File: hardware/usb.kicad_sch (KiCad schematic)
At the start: 7 parts, among them J4 USB_C_Receptacle_USB2.0_14P

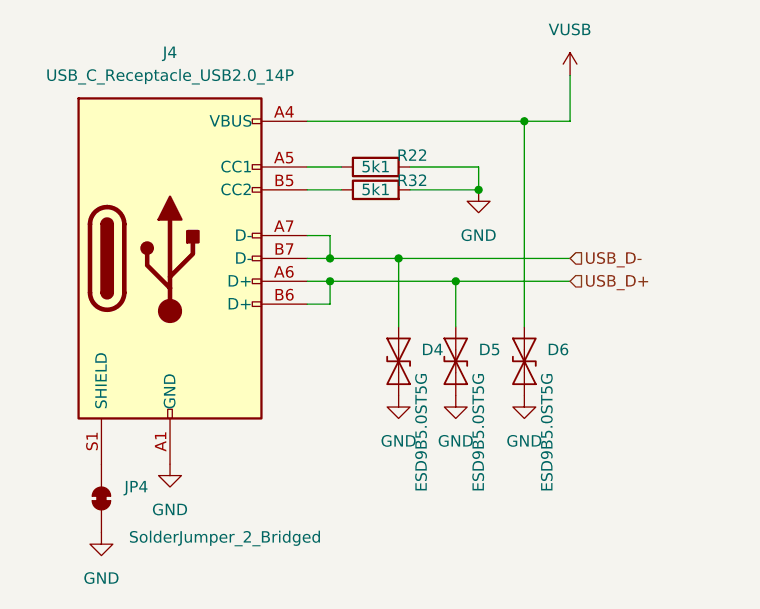
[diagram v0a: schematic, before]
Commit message: update usb port, esd, lcsc
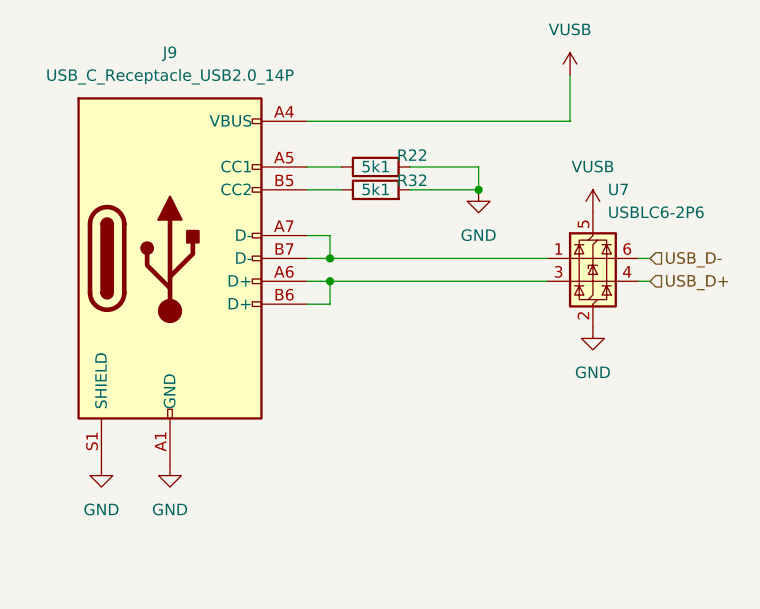
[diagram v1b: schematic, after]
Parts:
- removed D4, D5, D6: ESD9B5.0ST5G, Diode_SMD:D_SOD-923, symbol Diode:ESD9B5.0ST5G
- removed J4: USB_C_Receptacle_USB2.0_14P, Connector_USB:USB_C_Receptacle_GCT_USB4125-xx-x_6P_TopMnt_Horizontal, symbol Connector:USB_C_Receptacle_USB2.0_14P
- removed JP4: SolderJumper_2_Bridged, Jumper:SolderJumper-2_P1.3mm_Bridged_RoundedPad1.0x1.5mm, symbol Jumper:SolderJumper_2_Bridged
- added J9: USB_C_Receptacle_USB2.0_14P, Connector_USB:USB_C_Receptacle_GCT_USB4105-xx-A_16P_TopMnt_Horizontal, symbol Connector:USB_C_Receptacle_USB2.0_14P
- added U7: USBLC6-2P6, Package_TO_SOT_SMD:SOT-666, symbol Power_Protection:USBLC6-2P6
- R22, R32: footprint Resistor_SMD:R_0603_1608Metric -> Resistor_SMD:R_0402_1005Metric; LCSC (none) -> C25905
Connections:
- net GND: now also J9.A1 (GND), J9.A12 (GND), J9.B1 (GND), J9.B12 (GND), J9.S1 (SHIELD), U7.2 (GND)
- net USB_D+: now also U7.4 (I/O2)
- net USB_D-: now also U7.6 (I/O1)
- net VUSB: now also J9.A4 (VBUS), J9.A9 (VBUS), J9.B4 (VBUS), J9.B9 (VBUS), U7.5 (VBUS)
- net at R32.1: now also J9.B5 (CC2)
- net at R22.1: now also J9.A5 (CC1)
- new net: J9.A7 (D-), J9.B7 (D-), U7.1 (I/O1)
- new net: J9.A6 (D+), J9.B6 (D+), U7.3 (I/O2)

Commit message: lcd wires, wire direction
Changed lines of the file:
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@@
 	)
 	(hierarchical_label "USB_D-"
-		(shape input)
+		(shape bidirectional)
 		(at 149.86 90.17 0)
 		(fields_autoplaced yes)
@@
 	)
 	(hierarchical_label "USB_D+"
-		(shape input)
+		(shape bidirectional)
 		(at 149.86 92.71 0)
 		(fields_autoplaced yes)

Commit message: Associate all LCSC component
Change sdcard pullup resistor to 47K
Center main schematic
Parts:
- R22, R32: value 5k1 -> 5.1K
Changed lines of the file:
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@@
 			)
 		)
-		(property "Value" "5k1"
+		(property "Value" "5.1K"
 			(at 119.38 82.55 90)
 			(effects
@@
 			)
 		)
-		(property "Value" "5k1"
+		(property "Value" "5.1K"
 			(at 119.38 80.01 90)
 			(effects

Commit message: update bom, correct jlcpcb rotation
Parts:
- U7: JLCPCB Rotation Offset (none) -> 270
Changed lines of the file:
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@@
+			)
+		)
+		(property "JLCPCB Rotation Offset" "270"
+			(at 143.51 90.17 0)
+			(effects
+				(font
+					(size 1.27 1.27)
+				)
+				(hide yes)
 			)
 		)

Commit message: Fix rotation and position offset of components
Fix lora module rotation
Fix esp32 module position offset
Fix sd card position offset
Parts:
- J9: JLCPCB Position Offset (none) -> 0,1.3
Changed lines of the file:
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@@
+			)
+		)
+		(property "JLCPCB Position Offset" ""
+			(at 143.51 90.17 0)
+			(effects
+				(font
+					(size 1.27 1.27)
+				)
+				(hide yes)
 			)
 		)
@@
 			)
 		)
+		(property "JLCPCB Position Offset" ""
+			(at 119.38 82.55 0)
+			(effects
+				(font
+					(size 1.27 1.27)
+				)
+				(hide yes)
+			)
+		)
 		(pin "1"
 		)
@@
 			)
 		)
+		(property "JLCPCB Position Offset" ""
+			(at 119.38 80.01 0)
+			(effects
+				(font
+					(size 1.27 1.27)
+				)
+				(hide yes)
+			)
+		)
 		(pin "1"
 		)
@@
 			(at 96.52 90.17 0)
 			(effects
+				(font
+					(size 1.27 1.27)
+				)
+				(hide yes)
+			)
+		)
+		(property "JLCPCB Position Offset" "0,1.3"
+			(at 96.52 90.17 0)
+			(effects
